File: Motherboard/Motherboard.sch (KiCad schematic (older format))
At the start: 188 parts, among them J1 Jack-DC_18v, J2 65SIB_Connector, J3 DB9_Header, J4 GPIO_Connector, J5 Expansion_Connector, J6 Expansion_Connector, J7 Expansion_Connector, J8 Expansion_Connector, J9 Expansion_Connector, P1 POWER TERMINAL, Q1 2N3055, Q2 TIC106, SW1 SW_DPDT, SW2 FUSE RESET, SW3 PROCESSOR RESET, U1 LM7812_TO220, U13 LM386, U14 LM7912_TO220, U4 LM7805_TO220, X1 ACO-8MHz

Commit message: 420 traces to go...
420! 420!! 420!!!
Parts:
- added unit 3 of CLK_DIV1
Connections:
- net GND: now also CLK_DIV1.7 (GND)
- net VCC: now also CLK_DIV1.14 (VCC)
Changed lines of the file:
@@
 Text GLabel 25350 17150 3    50   Output ~ 0
 GND
+$Comp
+L 74xx:74HC74 CLK_DIV1
+U 3 1 627B16A5
+P 21250 17650
+F 0 "CLK_DIV1" H 21250 18131 50  0000 C CNN
+F 1 "74HC74" H 21250 18040 50  0000 C CNN
+F 2 "Package_DIP:DIP-14_W7.62mm_Socket_LongPads" H 21250 17650 50  0001 C CNN
+F 3 "74xx/74hc_hct74.pdf" H 21250 17650 50  0001 C CNN
+	3    21250 17650
+	1    0    0    -1
+$EndComp
+Text GLabel 21250 17250 1    50   Input ~ 0
+VCC
+Text GLabel 21250 18050 3    50   Output ~ 0
+GND
 $EndSCHEMATC

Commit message: 202 traces until 2.3...
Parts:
- 12v1: value 12v INDICATOR -> +12v INDICATOR
- 5v1: value 5v INDICATOR -> +5v INDICATOR
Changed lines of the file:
@@
 P 7050 2750
 F 0 "5v1" V 7089 2632 50  0000 R CNN
-F 1 "5v INDICATOR" V 6998 2632 50  0000 R CNN
+F 1 "+5v INDICATOR" V 6998 2632 50  0000 R CNN
 F 2 "LED_THT:LED_D5.0mm" H 7050 2750 50  0001 C CNN
 F 3 "~" H 7050 2750 50  0001 C CNN
@@
 P 7800 2750
 F 0 "12v1" V 7839 2632 50  0000 R CNN
-F 1 "12v INDICATOR" V 7748 2632 50  0000 R CNN
+F 1 "+12v INDICATOR" V 7748 2632 50  0000 R CNN
 F 2 "LED_THT:LED_D5.0mm" H 7800 2750 50  0001 C CNN
 F 3 "~" H 7800 2750 50  0001 C CNN

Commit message: Finished routing traces...
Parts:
- CLK_DIV1: value 74HC74 -> 74HCT74
- CS_65SIB_AND1, CS_GPIO_AND1, CS_UART_AND1, IRQ_RW_AND1: value 74LS08 -> 74HCT08
- CS_65SIB_AND4, CS_GPIO_AND4, CS_UART_AND4: value 74LS21 -> 74HCT21
- IRQ_DECODE1: value 74LS148 -> 74HCT148
- IRQ_OUT1: value 74LS85 -> 74HCT85
- ROM1_NAND4, ROM2_NAND4, ROM3_NAND4, ROM4_NAND4, SHARED_ROM2: value 74LS20 -> 74HCT20
- ~CS_DEV1: value 74LS138 -> 74HCT138
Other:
- note added: "IRQ Priority and handling registers\nAddress space: 0xD000"
- note removed: "IRQ Priority and handling registers"

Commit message: 2.3 has arrived...
2.3! 2.3!! 2.3!!!
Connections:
- net VCC: now also CLK_DIV1.11 (C), CLK_DIV1.2 (D), CLK_DIV1.6 (~Q); no longer CLK_DIV1.1 (~R), CLK_DIV1.13 (~R)
- new net: CLK_DIV1.1 (~R), CLK_DIV1.13 (~R)
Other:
- moved on the sheet: C10, C11, C12, C13, C14, C15, C16, C17, C18, C19, C20, C21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

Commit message: Bug fixes...
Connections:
- net VCC: now also CLK_DIV1.1 (~R), CLK_DIV1.13 (~R); no longer CLK_DIV1.11 (C), CLK_DIV1.2 (D), CLK_DIV1.6 (~Q)
- new net: CLK_DIV1.11 (C), CLK_DIV1.2 (D), CLK_DIV1.6 (~Q)
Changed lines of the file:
@@
 	6800 8150 6800 8450
 Wire Wire Line
-	6800 8450 6650 8450
-Wire Wire Line
 	5650 8450 5650 7950
 Wire Wire Line
@@
 Wire Wire Line
 	7300 8400 7300 8350
-Wire Wire Line
-	6650 8450 6650 8600
-Text GLabel 6650 8600 3    50   Input ~ 0
+Text GLabel 6650 8550 3    50   Input ~ 0
 VCC
 $Comp
@@
 Wire Wire Line
 	6650 7500 7300 7500
-Connection ~ 6650 8450
 Wire Wire Line
-	6650 8450 5650 8450
+	6250 8400 6650 8400
+Connection ~ 6650 8400
+Wire Wire Line
+	6650 8400 7300 8400
+Wire Wire Line
+	5650 8450 6800 8450
 Wire Wire Line
-	6250 8400 7300 8400
+	6650 8400 6650 8550
 $EndSCHEMATC

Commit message: Bug fixes and shutdown button added...
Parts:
- removed FUSE_DISABLE1: Jumper_2_Open, Connector_PinHeader_2.54mm:PinHeader_1x02_P2.54mm_Vertical, symbol Jumper:Jumper_2_Open
- added SW3: SHUTDOWN, Button_Switch_THT:SW_PUSH_6mm_H4.3mm, symbol Switch:SW_Push
- R12: value 700 Ω -> 16 Ω
- renumbered SW3 to SW4
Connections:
- net FUSE_IN: now also SW3.1
- net FUSE_OUT: now also SW3.2
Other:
- moved on the sheet: Q1, Q2, R12, R15, SW2
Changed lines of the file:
@@
 	3650 7850 3650 8100
 $Comp
-L Switch:SW_Push SW3
+L Switch:SW_Push SW4
 U 1 1 6196BAC3
 P 2200 8300
-F 0 "SW3" V 2154 8448 50  0000 L CNN
+F 0 "SW4" V 2154 8448 50  0000 L CNN
 F 1 "PROCESSOR RESET" V 2245 8448 50  0000 L CNN
 F 2 "Button_Switch_THT:SW_PUSH_6mm_H4.3mm" H 2200 8500 50  0001 C CNN
@@
 U 1 1 63132134
 P 5750 3900
-F 0 "U13" H 6094 3946 50  0000 L CNN
-F 1 "LM386" H 6094 3855 50  0000 L CNN
+F 0 "U13" H 5900 4100 50  0000 L CNN
+F 1 "LM386" H 5850 4000 50  0000 L CNN
 F 2 "Package_DIP:DIP-8_W7.62mm_LongPads" H 5850 4000 50  0001 C CNN
 F 3 "http://www.ti.com/lit/ds/symlink/lm386.pdf" H 5950 4100 50  0001 C CNN
@@
 L Transistor_BJT:2N3055 Q1
 U 1 1 61AC3338
-P 3100 3500
-F 0 "Q1" V 3428 3500 50  0000 C CNN
-F 1 "2N3055" V 3337 3500 50  0000 C CNN
-F 2 "Package_TO_SOT_THT:TO-3" H 3300 3425 50  0001 L CIN
-F 3 "http://www.onsemi.com/pub_link/Collateral/2N3055-D.PDF" H 3100 3500 50  0001 L CNN
-	1    3100 3500
+P 3150 3650
+F 0 "Q1" V 3478 3650 50  0000 C CNN
+F 1 "2N3055" V 3387 3650 50  0000 C CNN
+F 2 "Package_TO_SOT_THT:TO-3" H 3350 3575 50  0001 L CIN
+F 3 "http://www.onsemi.com/pub_link/Collateral/2N3055-D.PDF" H 3150 3650 50  0001 L CNN
+	1    3150 3650
 	0    -1   -1   0
 $EndComp
@@
 L Triac_Thyristor:TIC106 Q2
 U 1 1 61AC61D5
-P 2800 3700
-F 0 "Q2" V 3025 3700 50  0000 C CNN
-F 1 "TIC106" V 2934 3700 50  0000 C CNN
-F 2 "Package_TO_SOT_THT:TO-220-3_Horizontal_TabDown" H 2900 3625 50  0001 L CIN
-F 3 "http://pdf.datasheetcatalog.com/datasheet/PowerInnovations/mXyzrtvs.pdf" H 2800 3700 50  0001 L CNN
-	1    2800 3700
+P 2850 3850
+F 0 "Q2" V 3050 3850 50  0000 C CNN
+F 1 "TIC106" V 2950 3850 50  0000 C CNN
+F 2 "Package_TO_SOT_THT:TO-220-3_Horizontal_TabDown" H 2950 3775 50  0001 L CIN
+F 3 "http://pdf.datasheetcatalog.com/datasheet/PowerInnovations/mXyzrtvs.pdf" H 2850 3850 50  0001 L CNN
+	1    2850 3850
 	0    -1   -1   0
 $EndComp
@@
 L Switch:SW_Push SW2
 U 1 1 61ACCAEF
-P 2550 4350
-F 0 "SW2" H 2550 4635 50  0000 C CNN
-F 1 "FUSE RESET" H 2550 4544 50  0000 C CNN
-F 2 "Button_Switch_THT:SW_PUSH_6mm_H4.3mm" H 2550 4550 50  0001 C CNN
-F 3 "~" H 2550 4550 50  0001 C CNN
-	1    2550 4350
+P 2600 4400
+F 0 "SW2" H 2600 4685 50  0000 C CNN
+F 1 "FUSE RESET" H 2600 4594 50  0000 C CNN
+F 2 "Button_Switch_THT:SW_PUSH_6mm_H4.3mm" H 2600 4600 50  0001 C CNN
+F 3 "~" H 2600 4600 50  0001 C CNN
+	1    2600 4400
 	1    0    0    -1
 $EndComp
 Wire Wire Line
-	2750 4350 2900 4350
-Wire Wire Line
-	2900 4350 2900 4250
+	2800 4400 2950 4400
 Wire Wire Line
-	3100 3700 2950 3700
+	2950 4400 2950 4300
 Wire Wire Line
-	2350 3700 2650 3700
+	3150 3850 3000 3850
 Wire Wire Line
-	2350 3400 2900 3400
-Connection ~ 2350 3700
+	2400 3850 2700 3850
+Connection ~ 2400 3850
 $Comp
 L Device:R R12
 U 1 1 61C77788
-P 3350 3700
-F 0 "R12" V 3557 3700 50  0000 C CNN
-F 1 "700 Ω" V 3466 3700 50  0000 C CNN
-F 2 "Resistor_THT:R_Axial_DIN0207_L6.3mm_D2.5mm_P7.62mm_Horizontal" V 3280 3700 50  0001 C CNN
-F 3 "~" H 3350 3700 50  0001 C CNN
-	1    3350 3700
+P 3400 3850
+F 0 "R12" V 3607 3850 50  0000 C CNN
+F 1 "16 Ω" V 3516 3850 50  0000 C CNN
+F 2 "Resistor_THT:R_Axial_DIN0207_L6.3mm_D2.5mm_P7.62mm_Horizontal" V 3330 3850 50  0001 C CNN
+F 3 "~" H 3400 3850 50  0001 C CNN
+	1    3400 3850
 	0    -1   -1   0
 $EndComp
 Wire Wire Line
-	3300 3400 3600 3400
+	3350 3550 3650 3550
 Wire Wire Line
-	3600 3400 3600 3700
-Text GLabel 2250 3700 0    50   Input ~ 0
+	3650 3550 3650 3850
+Text GLabel 2300 3850 0    50   Input ~ 0
 FUSE_IN
-Text GLabel 3700 3700 2    50   Output ~ 0
+Text GLabel 3750 3850 2    50   Output ~ 0
 FUSE_OUT
 Wire Wire Line
-	3200 3700 3100 3700
-Connection ~ 3100 3700
+	3250 3850 3150 3850
+Connection ~ 3150 3850
 Wire Wire Line
-	3500 3700 3600 3700
-Connection ~ 3600 3700
+	3550 3850 3650 3850
+Connection ~ 3650 3850
 Wire Wire Line
 	5000 7600 5150 7600
@@
 L Device:R R15
 U 1 1 61ACF669
-P 2900 4100
-F 0 "R15" H 2970 4146 50  0000 L CNN
-F 1 "18k Ω" H 2970 4055 50  0000 L CNN
-F 2 "Resistor_THT:R_Axial_DIN0207_L6.3mm_D2.5mm_P7.62mm_Horizontal" V 2830 4100 50  0001 C CNN
-F 3 "~" H 2900 4100 50  0001 C CNN
-	1    2900 4100
+P 2950 4150
+F 0 "R15" H 3020 4196 50  0000 L CNN
+F 1 "18k Ω" H 3020 4105 50  0000 L CNN
+F 2 "Resistor_THT:R_Axial_DIN0207_L6.3mm_D2.5mm_P7.62mm_Horizontal" V 2880 4150 50  0001 C CNN
+F 3 "~" H 2950 4150 50  0001 C CNN
+	1    2950 4150
 	1    0    0    -1
 $EndComp
@@
 	5950 3100 6250 3100
 Wire Wire Line
-	2350 3400 2350 3700
-Wire Wire Line
-	2350 3700 2350 4350
-Wire Wire Line
-	2900 3950 2900 3850
-Wire Wire Line
 	5950 2200 5950 2550
 Wire Wire Line
@@
 	1800 4450 8750 4450
 Wire Wire Line
-	2250 3700 2350 3700
-Wire Wire Line
-	3600 3700 3700 3700
-Wire Wire Line
-	3600 3400 3600 3250
-Connection ~ 3600 3400
-Wire Wire Line
-	2500 3250 2350 3250
-Wire Wire Line
-	2350 3250 2350 3400
-Connection ~ 2350 3400
-$Comp
-L Jumper:Jumper_2_Open FUSE_DISABLE1
-U 1 1 631EF267
-P 2700 3250
-F 0 "FUSE_DISABLE1" H 2700 3350 50  0000 C CNN
-F 1 "Jumper_2_Open" H 2700 3150 50  0000 C CNN
-F 2 "Connector_PinHeader_2.54mm:PinHeader_1x02_P2.54mm_Vertical" H 2700 3250 50  0001 C CNN
-F 3 "~" H 2700 3250 50  0001 C CNN
-	1    2700 3250
-	1    0    0    -1
-$EndComp
+	2300 3850 2400 3850
 Wire Wire Line
-	3600 3250 2900 3250
+	3650 3850 3750 3850
 $Comp
 L 74xx:74HCT04 ROM_NOR1
@@
 Wire Wire Line
 	6650 8400 6650 8550
+$Comp
+L Switch:SW_Push SW3
+U 1 1 6280758E
+P 2750 3250
+F 0 "SW3" H 2750 3050 50  0000 C CNN
+F 1 "SHUTDOWN" H 2750 3150 50  0000 C CNN
+F 2 "Button_Switch_THT:SW_PUSH_6mm_H4.3mm" H 2750 3450 50  0001 C CNN
+F 3 "~" H 2750 3450 50  0001 C CNN
+	1    2750 3250
+	1    0    0    -1
+$EndComp
+Wire Wire Line
+	2400 3850 2400 4400
+Wire Wire Line
+	2950 3550 2400 3550
+Wire Wire Line
+	2400 3550 2400 3850
+Wire Wire Line
+	2550 3250 2400 3250
+Connection ~ 2400 3550
+Wire Wire Line
+	2950 3250 3650 3250
+Connection ~ 3650 3550
+Wire Wire Line
+	2400 3250 2400 3550
+Wire Wire Line
+	3650 3250 3650 3550
 $EndSCHEMATC

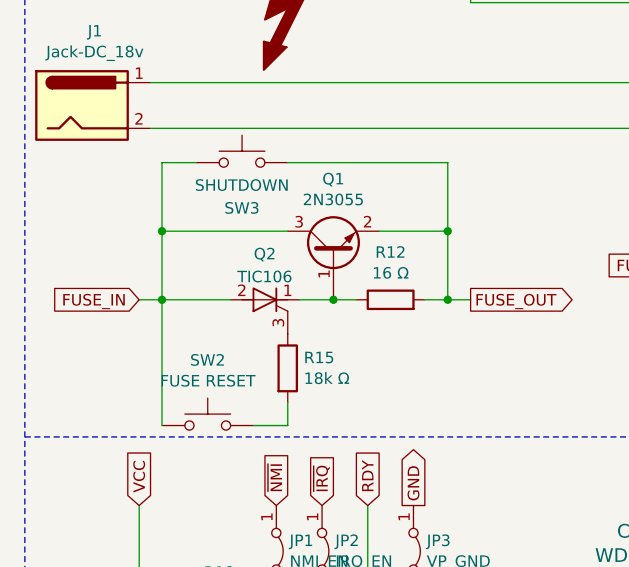
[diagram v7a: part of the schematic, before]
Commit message: Renamed some components...
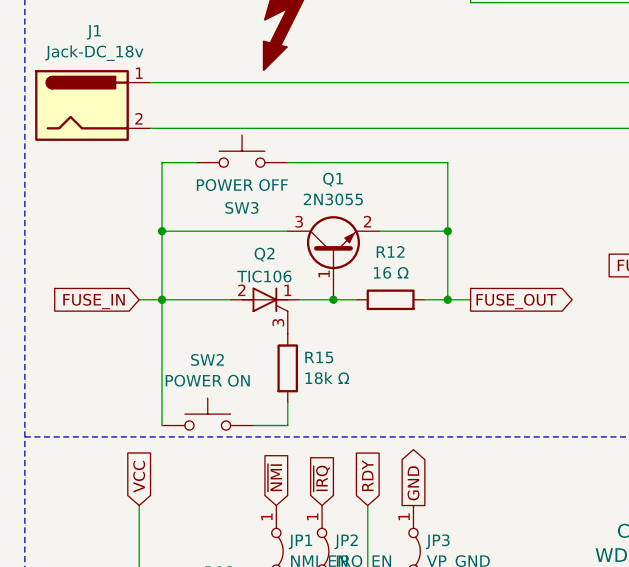
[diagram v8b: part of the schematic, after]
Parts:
- SW2: value FUSE RESET -> POWER ON
- SW3: value SHUTDOWN -> POWER OFF
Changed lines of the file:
@@
 P 2600 4400
 F 0 "SW2" H 2600 4685 50  0000 C CNN
-F 1 "FUSE RESET" H 2600 4594 50  0000 C CNN
+F 1 "POWER ON" H 2600 4594 50  0000 C CNN
 F 2 "Button_Switch_THT:SW_PUSH_6mm_H4.3mm" H 2600 4600 50  0001 C CNN
 F 3 "~" H 2600 4600 50  0001 C CNN
@@
 P 2750 3250
 F 0 "SW3" H 2750 3050 50  0000 C CNN
-F 1 "SHUTDOWN" H 2750 3150 50  0000 C CNN
+F 1 "POWER OFF" H 2750 3150 50  0000 C CNN
 F 2 "Button_Switch_THT:SW_PUSH_6mm_H4.3mm" H 2750 3450 50  0001 C CNN
 F 3 "~" H 2750 3450 50  0001 C CNN
